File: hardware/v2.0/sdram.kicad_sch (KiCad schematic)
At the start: 10 parts, among them U1 ECP5-CABGA256, U11 W9825G6KH

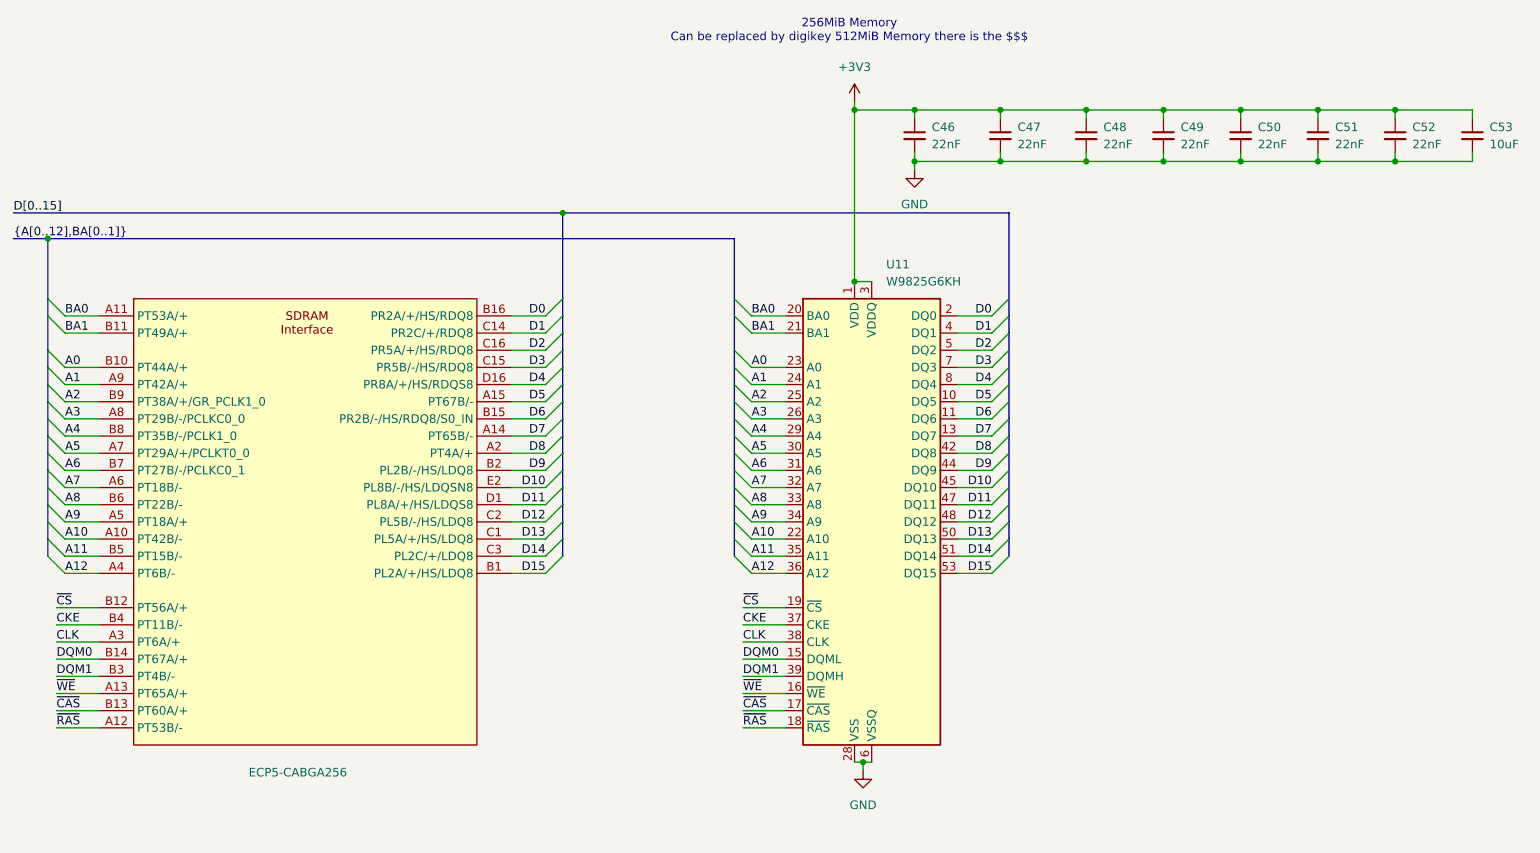
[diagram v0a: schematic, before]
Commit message: Added 54-TFPGA chip, front routing
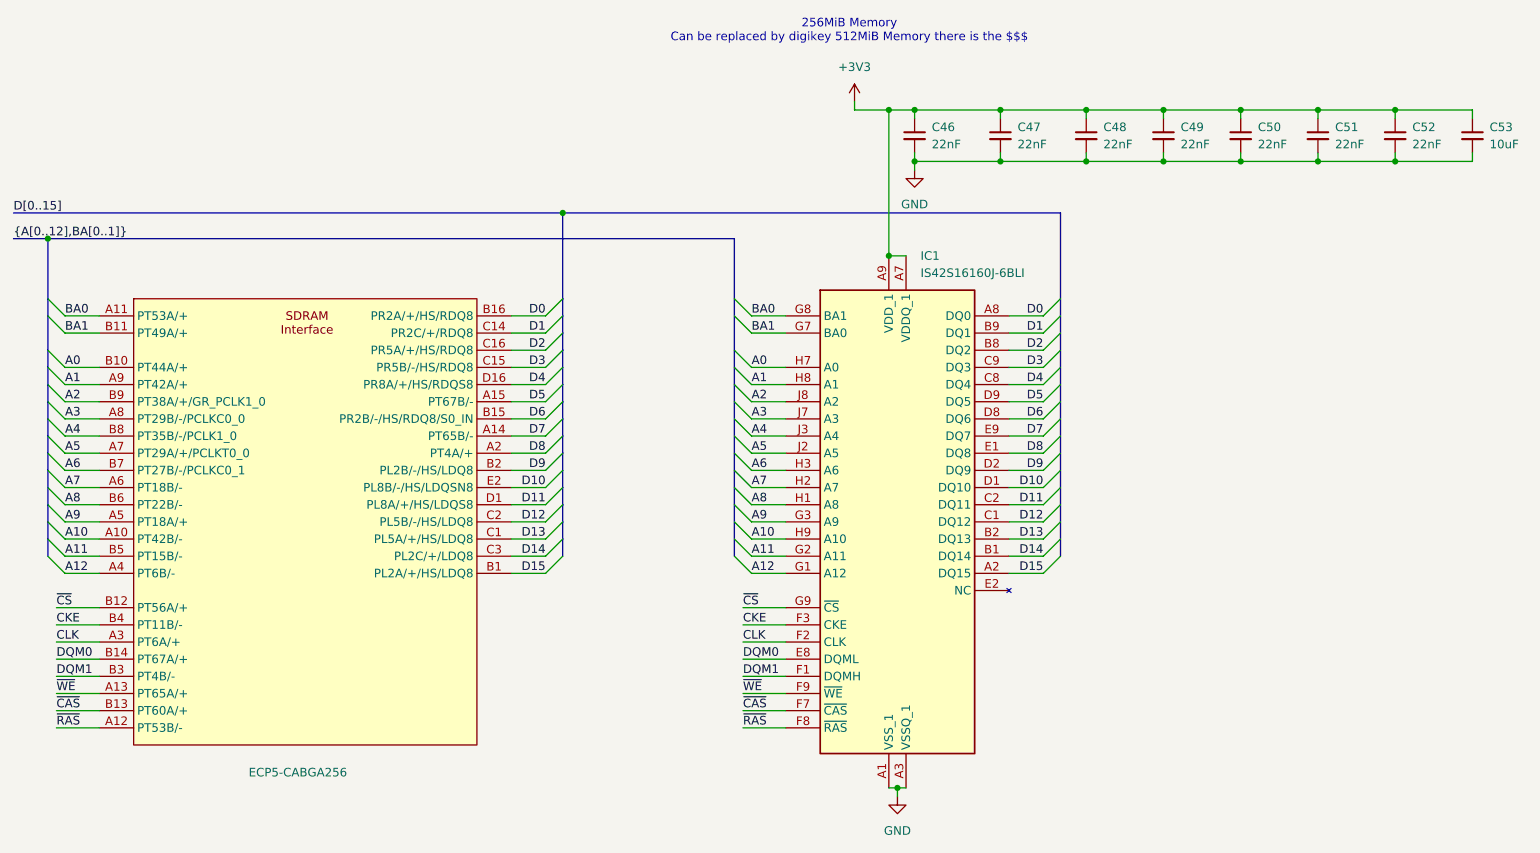
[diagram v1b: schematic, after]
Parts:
- removed U11: W9825G6KH, Package_SO:TSOP-II-54_22.2x10.16mm_P0.8mm, symbol Memory_RAM:MT48LC16M16A2P
- added IC1: IS42S16160J-6BLI, BGA54C80P9X9_800X800X120, symbol IS42S16160J-6BLI:IS42S16160J-6BLI
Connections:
- net +3V3: now also IC1.A7 (VDDQ_1), IC1.A9 (VDD_1), IC1.B3 (VDDQ_2), IC1.C7 (VDDQ_3), IC1.D3 (VDDQ_4), IC1.E7 (VDD_2), IC1.J9 (VDD_3)
- net A0: now also IC1.H7 (A0)
- net A1: now also IC1.H8 (A1)
- net A10: now also IC1.H9 (A10)
- net A11: now also IC1.G2 (A11)
- net A12: now also IC1.G1 (A12)
- net A2: now also IC1.J8 (A2)
- net A3: now also IC1.J7 (A3)
- net A4: now also IC1.J3 (A4)
- net A5: now also IC1.J2 (A5)
- net A6: now also IC1.H3 (A6)
- net A7: now also IC1.H2 (A7)
- net A8: now also IC1.H1 (A8)
- net A9: now also IC1.G3 (A9)
- net BA0: now also IC1.G8 (BA1)
- net BA1: now also IC1.G7 (BA0)
- net CKE: now also IC1.F3 (CKE)
- net CLK: now also IC1.F2 (CLK)
- net D0: now also IC1.A8 (DQ0)
- net D1: now also IC1.B9 (DQ1)
- net D10: now also IC1.D1 (DQ10)
- net D11: now also IC1.C2 (DQ11)
- net D12: now also IC1.C1 (DQ12)
- net D13: now also IC1.B2 (DQ13)
- net D14: now also IC1.B1 (DQ14)
- net D15: now also IC1.A2 (DQ15)
- net D2: now also IC1.B8 (DQ2)
- net D3: now also IC1.C9 (DQ3)
- net D4: now also IC1.C8 (DQ4)
- net D5: now also IC1.D9 (DQ5)
- net D6: now also IC1.D8 (DQ6)
- net D7: now also IC1.E9 (DQ7)
- net D8: now also IC1.E1 (DQ8)
- net D9: now also IC1.D2 (DQ9)
- net DQM0: now also IC1.E8 (DQML)
- net DQM1: now also IC1.F1 (DQMH)
- net GND: now also IC1.A1 (VSS_1), IC1.A3 (VSSQ_1), IC1.B7 (VSSQ_2), IC1.C3 (VSSQ_3), IC1.D7 (VSSQ_4), IC1.E3 (VSS_2), IC1.J1 (VSS_3)
- net ~{CAS}: now also IC1.F7 (~{CAS})
- net ~{CS}: now also IC1.G9 (~{CS})
- net ~{RAS}: now also IC1.F8 (~{RAS})
- net ~{WE}: now also IC1.F9 (~{WE})

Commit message: Authoring
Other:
- company: Chengyin Yao (cheyao) -> Chengyin Yao (cheyao), Vadym Vikulin
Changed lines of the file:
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@@
 	(title_block
 		(title "Icepi Zero")
-		(date "2025-10-10")
-		(rev "v1.3")
-		(company "Chengyin Yao (cheyao)")
+		(date "2026-01-05")
+		(rev "v2.0")
+		(company "Chengyin Yao (cheyao), Vadym Vikulin")
 		(comment 1 "https://github.com/cheyao/icepi-zero")
 		(comment 2 "License: Solderpad")
